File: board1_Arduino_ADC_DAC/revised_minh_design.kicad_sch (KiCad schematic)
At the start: 36 parts, among them J1 Conn_01x03_Male, J2 Conn_02x08_Odd_Even, J3 Conn_02x08_Odd_Even, J4 Conn_02x08_Odd_Even, J5 Conn_01x02_Male, U1 ESP32-DevKit-C, U2 LM7805_TO220, U3 MCP1754S-3302xCB, U4 MCP1825S-3.3V, U5 MCP1501-33xSN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

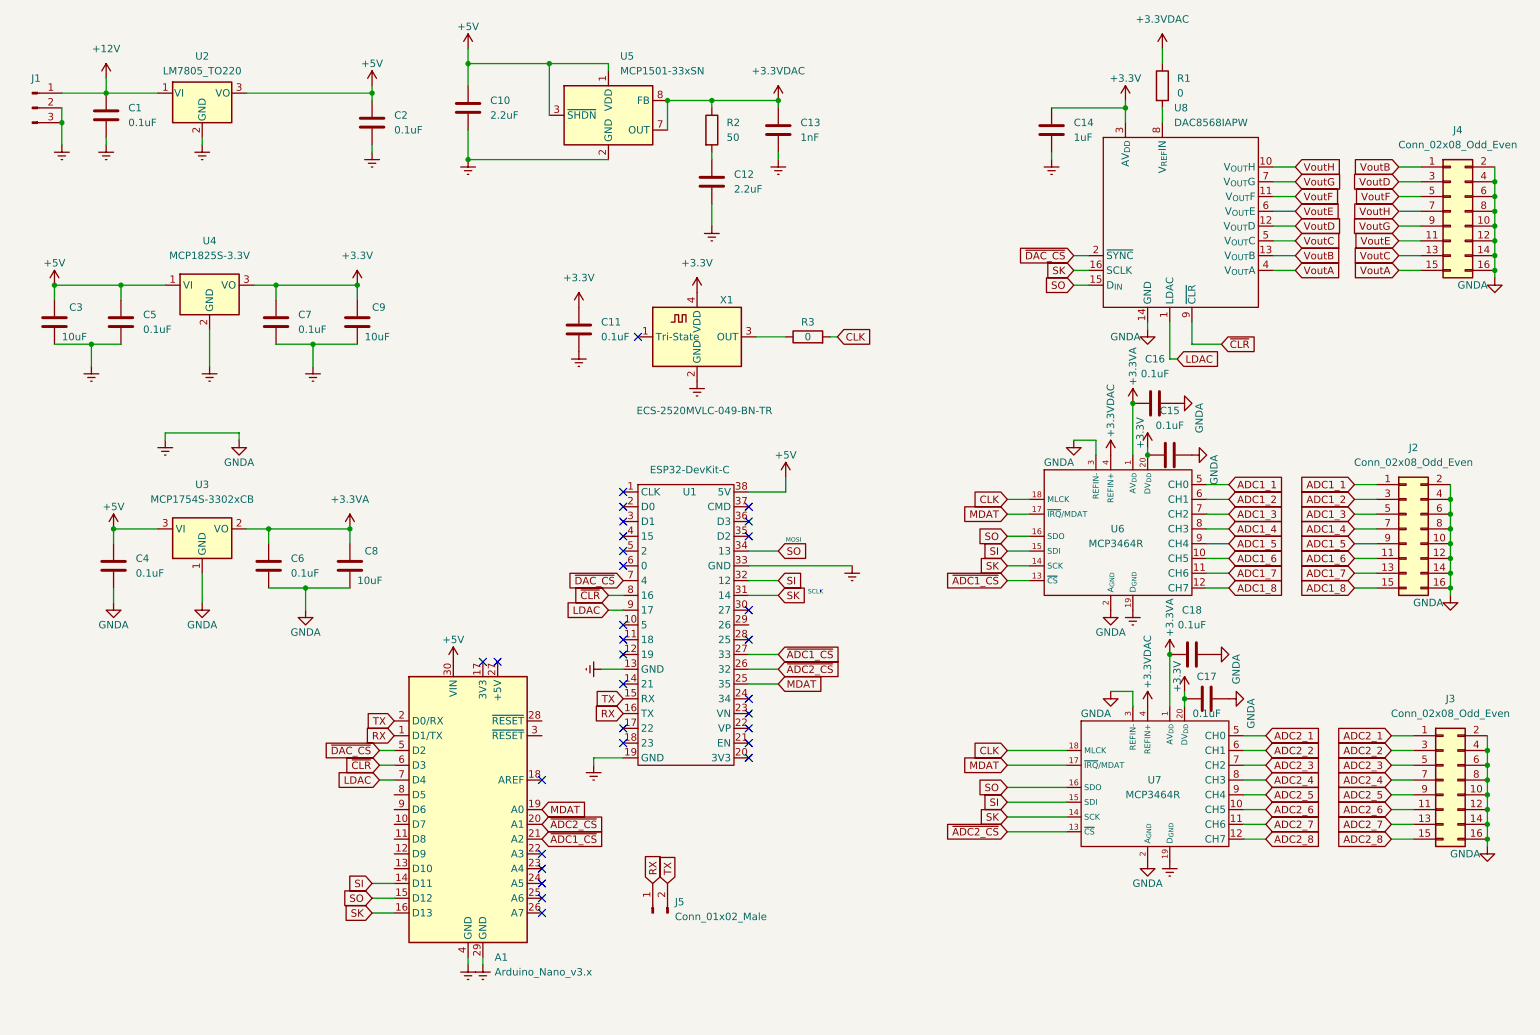
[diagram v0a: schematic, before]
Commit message: exported STEP file. Minor changes to schematics for better documentations
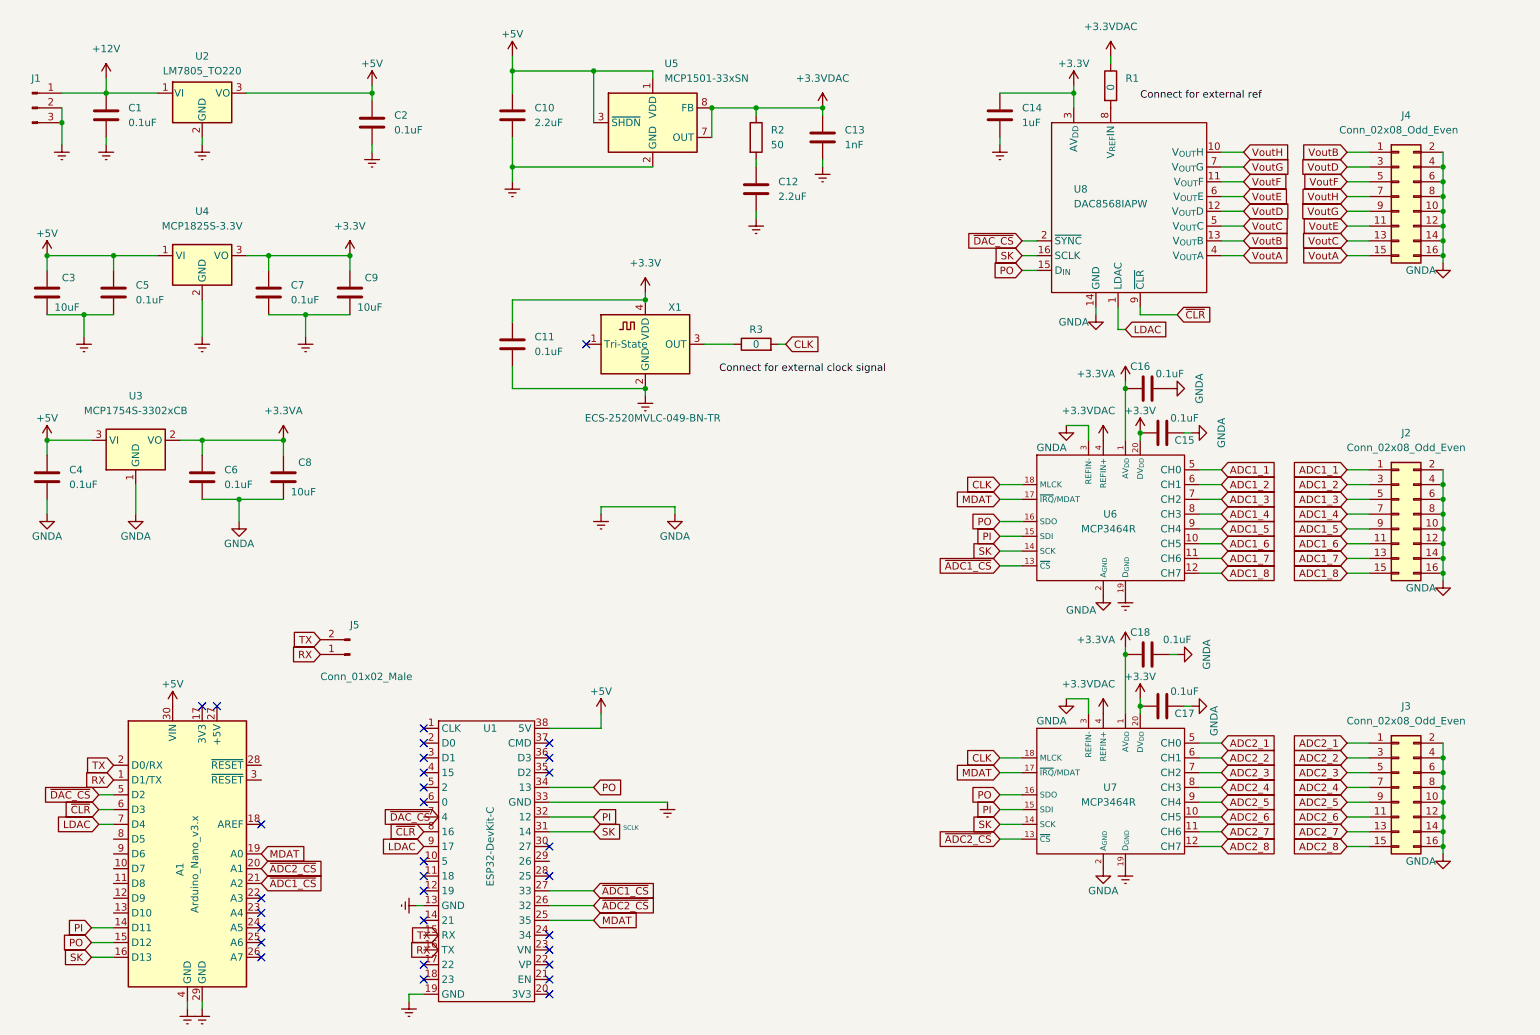
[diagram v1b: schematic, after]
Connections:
- net RX: no longer U1.16 (TX)
- net TX: no longer U1.15 (RX)
- net ~{DAC_CS}: no longer U1.7 (4)
- net SI renamed PI
- net SO renamed PO
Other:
- note removed: "MOSI"
- title: (none) -> S.H.V.R.I.M.P.S.    16 channels data acquisition device
- moved on the sheet: A1, C10, C11, C12, C13, C14, C15, C16, C17, C18, C3, C4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

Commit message: Fixed PI PO, DAC port ordering, MDAT Pin, clock connection
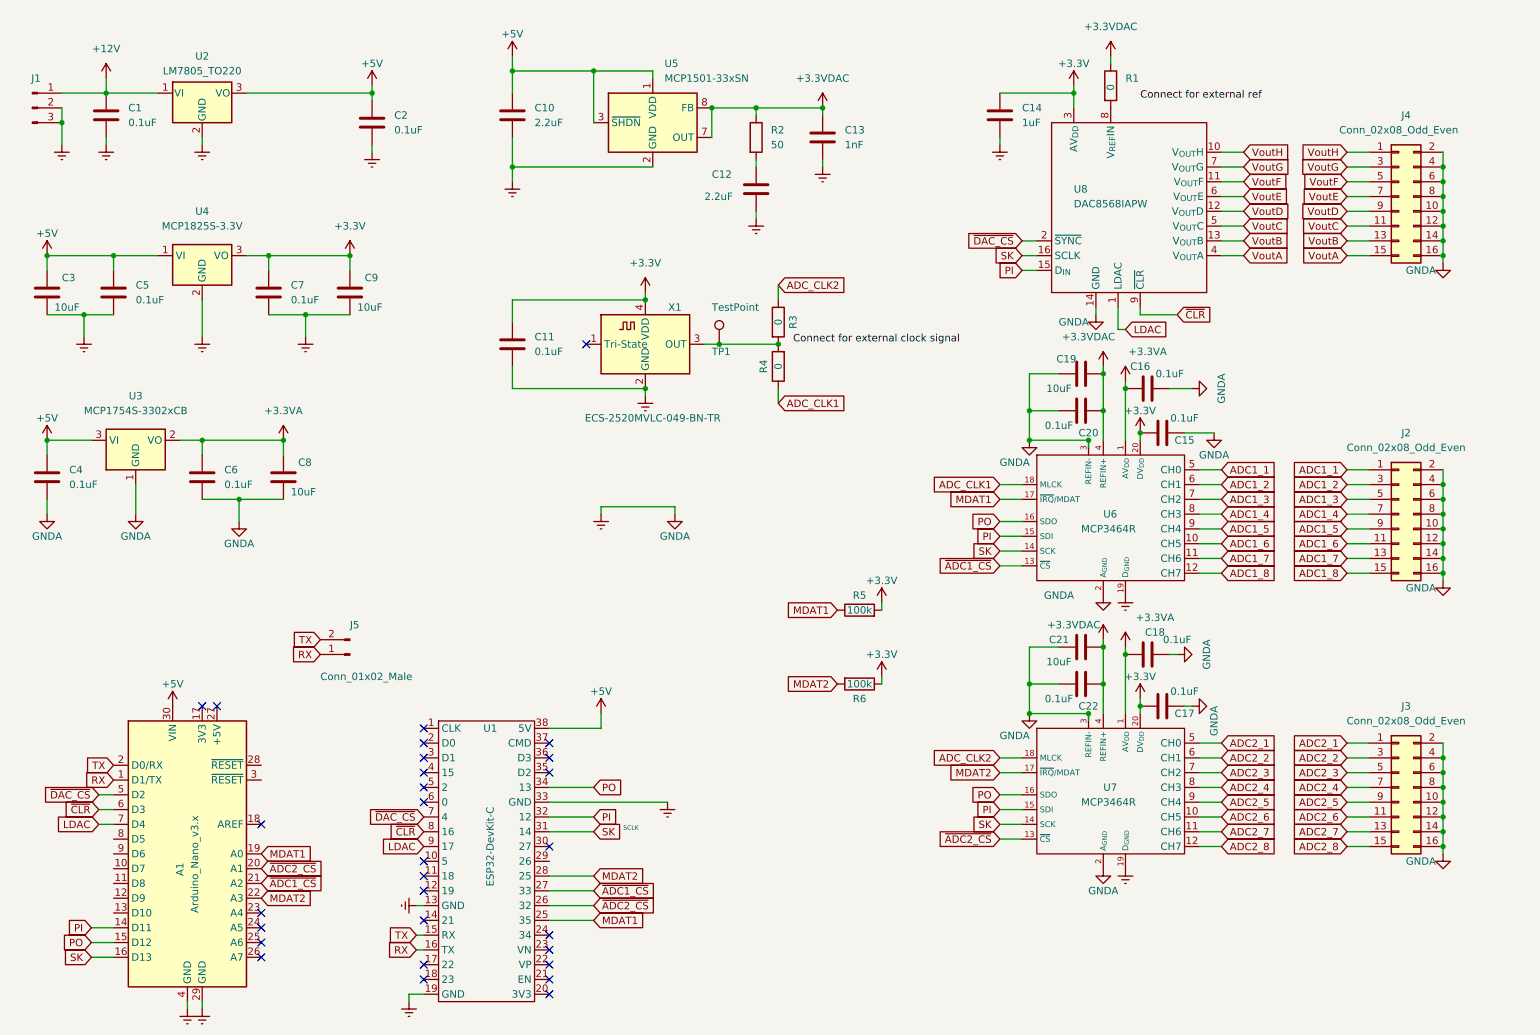
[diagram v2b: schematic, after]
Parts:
- added C19, C21: 10uF, Capacitor_SMD:C_0805_2012Metric_Pad1.18x1.45mm_HandSolder, symbol Device:C
- added C20, C22: 0.1uF, Capacitor_SMD:C_0805_2012Metric_Pad1.18x1.45mm_HandSolder, symbol Device:C
- added R4: 0, Resistor_SMD:R_0805_2012Metric_Pad1.20x1.40mm_HandSolder, symbol Device:R
- added R5, R6: 100k, Resistor_SMD:R_0805_2012Metric_Pad1.20x1.40mm_HandSolder, symbol Device:R
- added TP1: TestPoint, Connector_PinHeader_2.54mm:PinHeader_1x01_P2.54mm_Vertical, symbol Connector:TestPoint
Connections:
- net +3.3VDAC: now also C19.1, C20.1, C21.1, C22.1
- net +3V3: now also R5.2, R6.1
- net Earth: now also C19.2, C20.2, C21.2, C22.2
- net PI: now also U8.15 (D_{IN})
- net PO: no longer U8.15 (D_{IN})
- net RX: now also U1.16 (TX)
- net TX: now also U1.15 (RX)
- net VoutB: now also J4.13 (Pin_13); no longer J4.1 (Pin_1)
- net VoutC: now also J4.11 (Pin_11); no longer J4.13 (Pin_13)
- net VoutD: now also J4.9 (Pin_9); no longer J4.3 (Pin_3)
- net VoutE: now also J4.7 (Pin_7); no longer J4.11 (Pin_11)
- net VoutG: now also J4.3 (Pin_3); no longer J4.9 (Pin_9)
- net VoutH: now also J4.1 (Pin_1); no longer J4.7 (Pin_7)
- net ~{DAC_CS}: now also U1.7 (4)
- net at X1.3 (OUT): now also R3.2, R4.2, TP1.1; no longer R3.1
- net MDAT2: now reaches A1.22 (A3)
- net MDAT2: now also U1.28 (25), U7.17 (~{IRQ}/MDAT), R6.2
- removed net CLK: R3.2, U6.18 (MLCK), U7.18 (MLCK)
- net MDAT renamed MDAT1
- net MDAT1: now also R5.1; no longer U7.17 (~{IRQ}/MDAT)
- new net ADC_CLK1: R4.1, U6.18 (MLCK)
- new net ADC_CLK2: R3.1, U7.18 (MLCK)
- no-connect marks 31 -> 29
